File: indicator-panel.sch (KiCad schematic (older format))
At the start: 73 parts, among them J101 Power In, P101 Data In, P102 Data Out, P103 Power In, P104 Power Out, U101 MAX3293, U102 STP16CP05, U103 STP16CP05, U106 STP16CP05, U108 LD1117S33CTR, U109 MAX3280, U110 MAX3280, U111 MAX3280

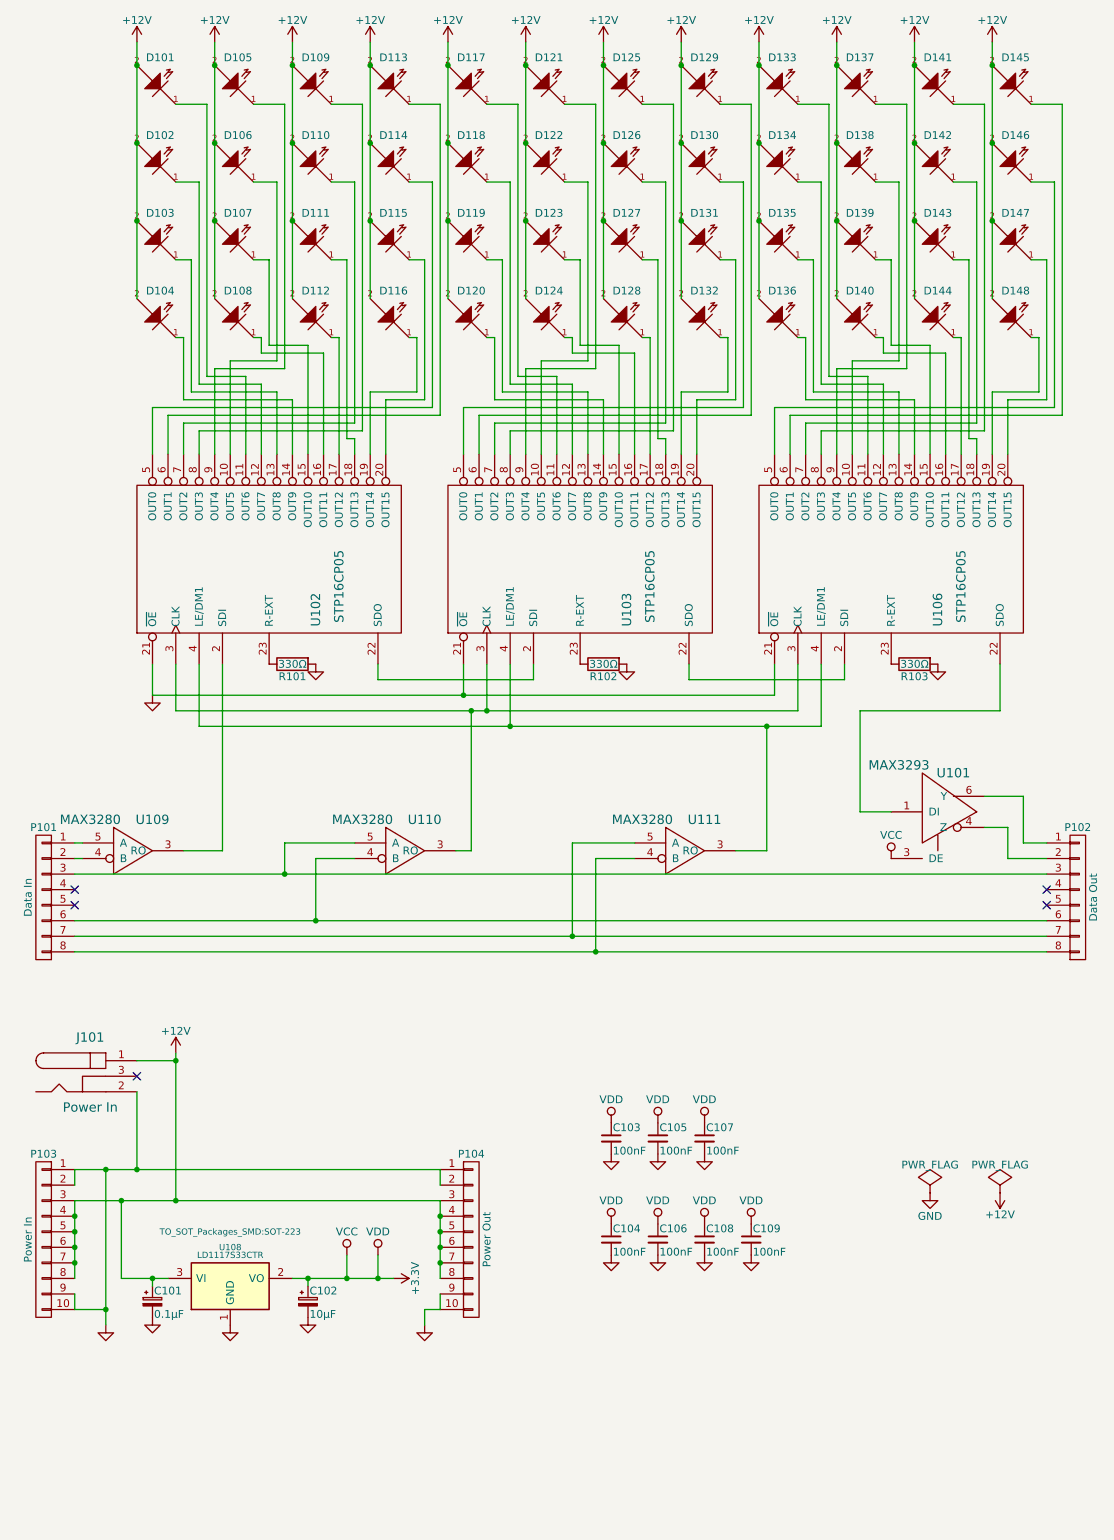
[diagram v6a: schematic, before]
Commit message: Changed to version 2.0 with the blanking signal and using a 4-unit rs485 receiver and transmitter.
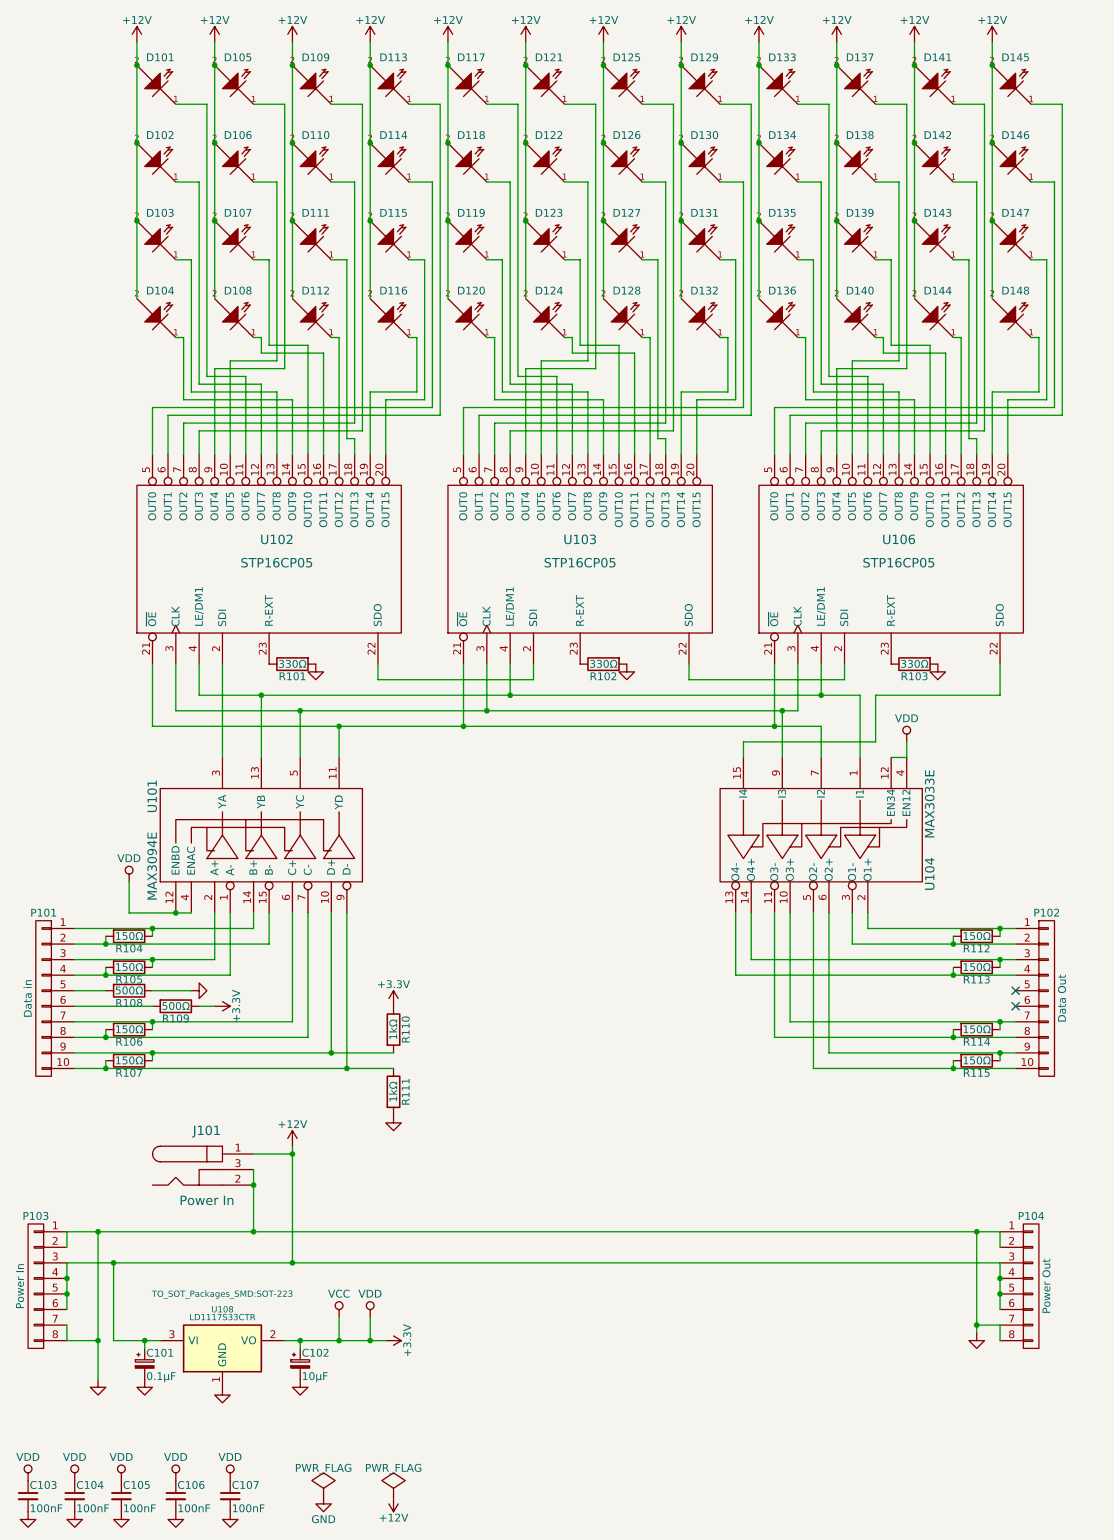
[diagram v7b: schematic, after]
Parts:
- removed C108, C109: 100nF, Capacitors_SMD:C_0805_HandSoldering, symbol C_Small
- removed P101: Data In, Pin_Headers:Pin_Header_Angled_2x04, symbol CONN_01X08
- removed P102: Data Out, Socket_Strips:Socket_Strip_Angled_2x04, symbol CONN_01X08
- removed P103: Power In, Pin_Headers:Pin_Header_Angled_2x05, symbol CONN_01X10
- removed P104: Power Out, Socket_Strips:Socket_Strip_Angled_2x05, symbol CONN_01X10
- removed U101: MAX3293, TO_SOT_Packages_SMD:SOT-23-6, symbol MAX3294
- removed U109, U110, U111: MAX3280, TO_SOT_Packages_SMD:SOT-23-5, symbol MAX3280
- added P101: Data in, Pin_Headers:Pin_Header_Angled_2x05, symbol CONN_01X10
- added P102: Data Out, Socket_Strips:Socket_Strip_Angled_2x05, symbol CONN_01X10
- added P103: Power In, Pin_Headers:Pin_Header_Angled_2x04, symbol CONN_01X08
- added P104: Power Out, Socket_Strips:Socket_Strip_Angled_2x04, symbol CONN_01X08
- added R104, R105, R106, R107, R112, R113, R114, R115: 150Ω, Resistors_SMD:R_0805, symbol R
- added R108, R109: 500Ω, Resistors_SMD:R_0805, symbol R
- added R110, R111: 1kΩ, Resistors_SMD:R_0805, symbol R
- added U101: MAX3094E, Housings_SOIC:SOIC-16_3.9x9.9mm_Pitch1.27mm, symbol MAX3094E
- added U104: MAX3033E, Housings_SOIC:SOIC-16_3.9x9.9mm_Pitch1.27mm, symbol MAX3033E
- C103, C104, C105, C106, C107: footprint Capacitors_SMD:C_0805_HandSoldering -> Capacitors_SMD:C_0805
- D101, D102, D103, D104, D105, D106, D107, D108, D109, D110, D111, D112, D113, D114, D115, D116, D117, D118, D119, D120, D121, D122, D123, D124, D125, D126, D127, D128, D129, D130, D131, D132, D133, D134, D135, D136, D137, D138, D139, D140, D141, D142, D143, D144, D145, D146, D147, D148: footprint myMods.pretty:LED_SMDuniversal_0805to1206 -> LEDs:LED-0805
- R101, R102, R103: footprint Resistors_SMD:R_0805_HandSoldering -> Resistors_SMD:R_0805
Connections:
- net +12V: now also P103.3 (P3), P103.4 (P4), P103.5 (P5), P103.6 (P6), P104.3 (P3), P104.4 (P4), P104.5 (P5), P104.6 (P6)
- net +3V3: now also R109.1, R110.1, U101.12 (ENBD), U101.16 (VDD), U101.4 (ENAC), U104.12 (EN34), U104.16 (VDD), U104.4 (EN12)
- net GND: now also J101.3, P103.1 (P1), P103.2 (P2), P103.7 (P7), P103.8 (P8), P104.1 (P1), P104.2 (P2), P104.7 (P7), P104.8 (P8), R108.1, R111.2, U101.8 (GND), U104.8 (GND); no longer U102.21 (~OE), U103.21 (~OE), U106.21 (~OE)
- net at U102.2 (SDI): now also U101.3 (YA)
- net at U102.3 (CLK), U103.3 (CLK), U106.3 (CLK): now also U101.5 (YC), U104.9 (I3)
- net at U102.4 (LE/DM1), U103.4 (LE/DM1), U106.4 (LE/DM1): now also U101.13 (YB), U104.1 (I1)
- net at U106.22 (SDO): now also U104.15 (I4)
- new net: U101.11 (YD), U102.21 (~OE), U103.21 (~OE), U104.7 (I2), U106.21 (~OE)
- new net: P101.4 (P4), R105.2, U101.1 (A-)
- new net: P101.9 (P9), R107.1, R110.2, U101.10 (D+)
- new net: P101.1 (P1), R104.1, U101.14 (B+)
- new net: P101.2 (P2), R104.2, U101.15 (B-)
- new net: P101.3 (P3), R105.1, U101.2 (A+)
- new net: P101.7 (P7), R106.1, U101.6 (C+)
- new net: P101.8 (P8), R106.2, U101.7 (C-)
- new net: P101.10 (P10), R107.2, R111.1, U101.9 (D-)
- new net: P101.5 (P5), R108.2
- new net: P101.6 (P6), R109.2
- new net: P102.1 (P1), R112.1, U104.2 (O1+)
- new net: P102.10 (P10), R115.2, U104.5 (O2-)
- new net: P102.2 (P2), R112.2, U104.3 (O1-)
- new net: P102.3 (P3), R113.1, U104.14 (O4+)
- new net: P102.4 (P4), R113.2, U104.13 (O4-)
- new net: P102.7 (P7), R114.1, U104.10 (O3+)
- new net: P102.8 (P8), R114.2, U104.11 (O3-)
- new net: P102.9 (P9), R115.1, U104.6 (O2+)
- no-connect marks 5 -> 2
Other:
- moved on the sheet: C101, C102, C103, C104, C105, C106, C107, J101, U108

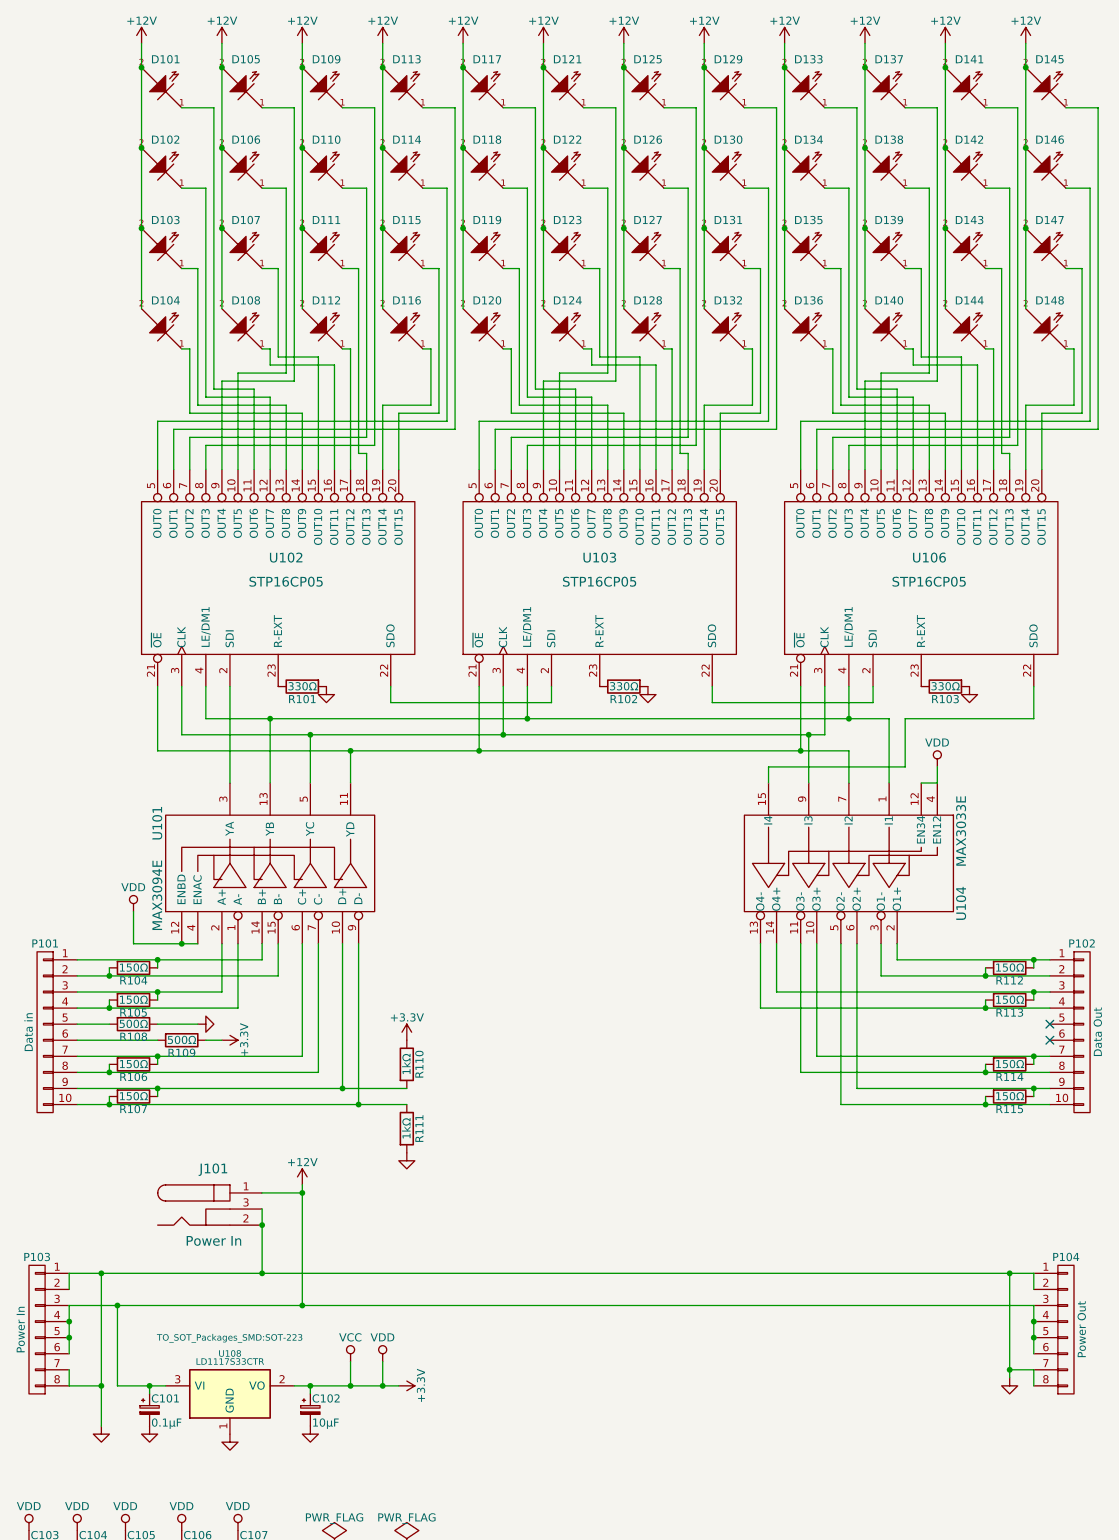
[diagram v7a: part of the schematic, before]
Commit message: Updated current limiting resistor to 3.3k
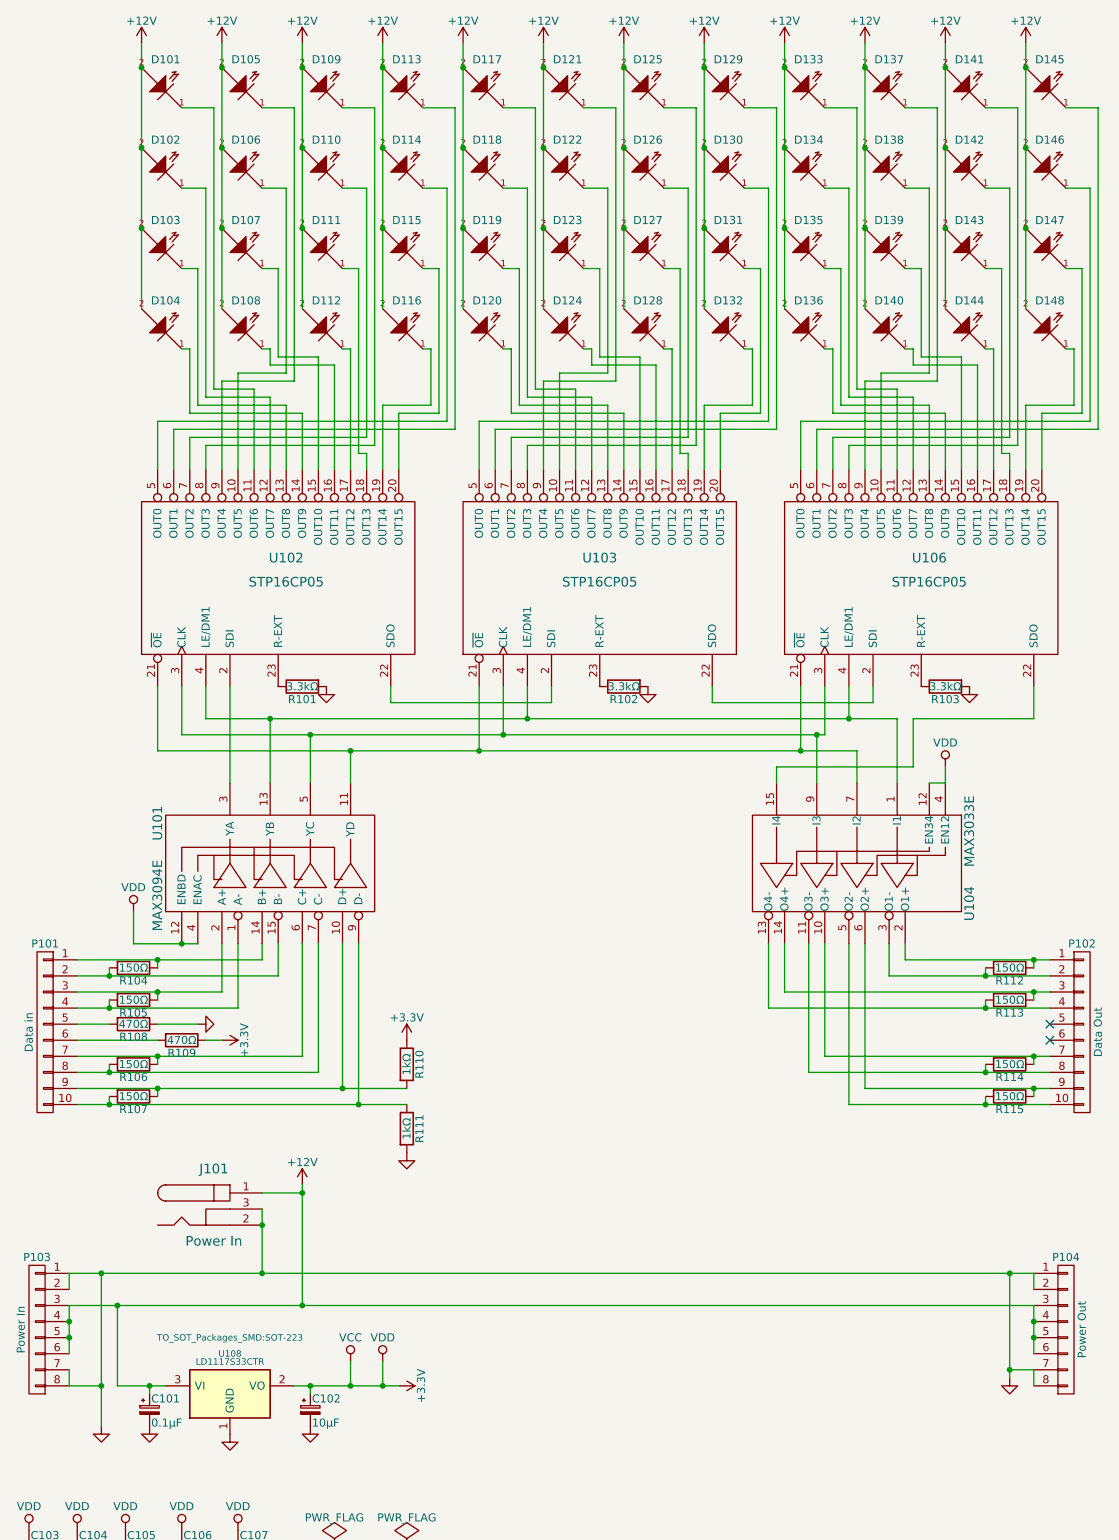
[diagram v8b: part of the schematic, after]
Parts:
- J101: footprint Connect:BARREL_JACK -> myMods.pretty:PJ-032B; manf# (none) -> PJ-032B
- R101, R102, R103: value 330Ω -> 3.3kΩ
- R104: manf# (none) -> RC0805JR-07150RL
- R108, R109: value 500Ω -> 470Ω; manf# (none) -> RC0805JR-07470RL
- R110: manf# (none) -> RC0805JR-071KL
- U101: manf# (none) -> MAX3094ECSE+
- U104: manf# (none) -> MAX3033ECSE+
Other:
- moved on the sheet: U104
